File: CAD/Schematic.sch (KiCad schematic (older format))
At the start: 4 parts

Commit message: Resiter value should be equal to the skin resitance value ~2MOhm is great.
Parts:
- removed I?: IDC, symbol Simulation_SPICE:IDC
- added D?: LED, symbol Device:LED
- added LS?: Speaker, symbol Device:Speaker
- added R2: 1M, symbol Device:R
- added U?: 4N35, Package_DIP:DIP-6_W7.62mm, symbol Isolator:4N35
- RotaryEncoder?: symbol OrangeRotaryEncoder:RotaryEncoder -> Schematic-rescue:RotaryEncoder-OrangeRotaryEncoder
- ShockPad?: symbol BhallaLabComponents:ShockPad -> Schematic-rescue:ShockPad-BhallaLabComponents
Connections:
- net labels added: CAM, GND, IMAGING_TRIG, LED, PAD+, PAD-, PUFF, TONE, VCC
- wire segments 8 -> 76
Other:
- note added: "1200 counts per cycle."
- note added: "CH1=CH3 \nCH2=CH4=~CH1\nImplemented in Arduino."
- note added: "PWM"
- note added: "To solenoid."

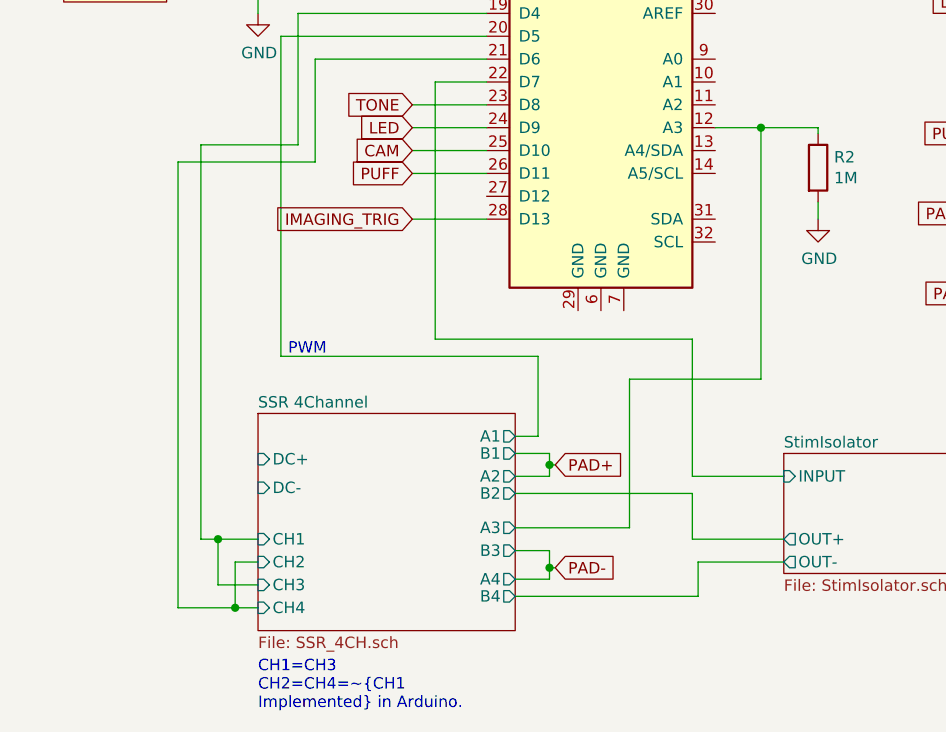
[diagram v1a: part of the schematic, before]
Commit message: Added missing projects.
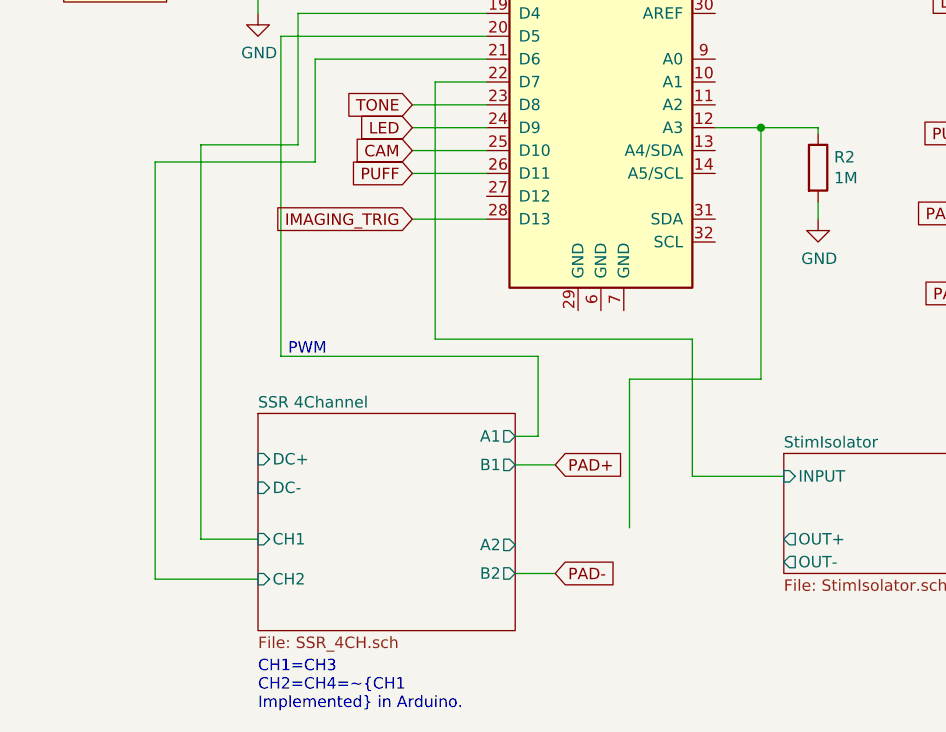
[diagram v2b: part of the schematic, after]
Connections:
- wire segments 76 -> 55
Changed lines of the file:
@@
 Wire Wire Line
 	5800 2900 6300 2900
-$Sheet
-S 5300 4750 1125 950
-U 5D1ADABF
-F0 "SSR 4Channel" 50
-F1 "SSR_4CH.sch" 50
-F2 "DC+" I L 5300 4950 50
-F3 "DC-" I L 5300 5075 50
-F4 "CH1" I L 5300 5300 50
-F5 "CH2" I L 5300 5400 50
-F6 "CH3" I L 5300 5500 50
-F7 "CH4" I L 5300 5600 50
-F8 "A1" O R 6425 4850 50
-F9 "B1" O R 6425 4925 50
-F10 "B2" O R 6425 5100 50
-F11 "A3" O R 6425 5250 50
-F12 "B3" O R 6425 5350 50
-F13 "A4" O R 6425 5475 50
-F14 "B4" O R 6425 5550 50
-F15 "A2" O R 6425 5025 50
-$EndSheet
 $Comp
 L Device:Speaker LS?
@@
 Wire Wire Line
 	5300 2800 5300 3000
-Wire Wire Line
-	5050 5300 5125 5300
-Wire Wire Line
-	5125 5300 5125 5500
-Wire Wire Line
-	5125 5500 5300 5500
-Connection ~ 5125 5300
-Wire Wire Line
-	5125 5300 5300 5300
-Wire Wire Line
-	5300 5400 5200 5400
-Wire Wire Line
-	5200 5400 5200 5600
-Connection ~ 5200 5600
-Wire Wire Line
-	5200 5600 5300 5600
 Text Notes 5300 6050 0    50   ~ 0
 CH1=CH3 \nCH2=CH4=~CH1\nImplemented in Arduino.
@@
 	5550 3200 5550 3650
 Wire Wire Line
-	5550 3650 4950 3650
-Wire Wire Line
-	4950 3650 4950 5600
-Wire Wire Line
 	5550 3200 6300 3200
-Wire Wire Line
-	4950 5600 5200 5600
-Wire Wire Line
-	6425 4925 6575 4925
-Wire Wire Line
-	6575 5025 6425 5025
-Wire Wire Line
-	6425 5350 6575 5350
-Wire Wire Line
-	6575 5475 6425 5475
 Wire Wire Line
 	5400 3100 5400 4500
@@
 Wire Wire Line
 	7500 3500 7300 3500
-Wire Wire Line
-	6575 5350 6575 5425
-Wire Wire Line
-	6575 4925 6575 4975
 $Comp
 L Schematic-rescue:ShockPad-BhallaLabComponents ShockPad?
@@
 Text GLabel 6600 4975 2    50   Input ~ 0
 PAD+
-Text GLabel 6600 5425 2    50   Input ~ 0
-PAD-
-Wire Wire Line
-	6600 4975 6575 4975
-Connection ~ 6575 4975
-Wire Wire Line
-	6575 4975 6575 5025
-Wire Wire Line
-	6600 5425 6575 5425
-Connection ~ 6575 5425
-Wire Wire Line
-	6575 5425 6575 5475
-Wire Wire Line
-	7600 5400 7225 5400
-Wire Wire Line
-	7225 5400 7225 5550
-Wire Wire Line
-	7225 5550 6425 5550
-Wire Wire Line
-	7600 5300 7200 5300
-Wire Wire Line
-	7200 5300 7200 5100
-Wire Wire Line
-	7200 5100 6425 5100
 Wire Wire Line
 	7200 4425 7200 5025
@@
 Wire Wire Line
 	6075 4425 7200 4425
-Wire Wire Line
-	6425 5250 6925 5250
 Wire Wire Line
 	6925 5250 6925 4600
@@
 Text Notes 5600 4500 2    50   ~ 0
 PWM
+Wire Wire Line
+	5050 5300 5300 5300
+Wire Wire Line
+	5300 5475 4850 5475
+Text GLabel 6600 5450 2    50   Input ~ 0
+PAD-
+$Sheet
+S 5300 4750 1125 950
+U 5D1ADABF
+F0 "SSR 4Channel" 50
+F1 "SSR_4CH.sch" 50
+F2 "DC+" I L 5300 4950 50
+F3 "DC-" I L 5300 5075 50
+F4 "CH1" I L 5300 5300 50
+F5 "CH2" I L 5300 5475 50
+F6 "A1" O R 6425 4850 50
+F7 "B1" O R 6425 4975 50
+F8 "B2" O R 6425 5450 50
+F9 "A2" O R 6425 5325 50
+$EndSheet
+Wire Wire Line
+	6425 5450 6600 5450
+Wire Wire Line
+	6425 4975 6600 4975
+Wire Wire Line
+	5550 3650 4850 3650
+Wire Wire Line
+	4850 3650 4850 5475
 $EndSCHEMATC

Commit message: Almost complete.
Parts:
- gave numbers to parts that had none: 2
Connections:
- wire segments 55 -> 73
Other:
- note added: "CH1=CH2 \nCH3=CH4=~CH1\nImplemented in Arduino."
- note added: "Not implemented.\nUsing as black-box."
- note added: "Resistance of mouse's paw is of the order of 1M.\nThe value of R2 must be the same."
- note removed: "CH1=CH3 \nCH2=CH4=~CH1\nImplemented in Arduino."
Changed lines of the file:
@@
 Sheet 1 3
 Title "Shocking Protocol"
-Date ""
-Rev "0.0.1"
-Comp "Bhalla Lab"
-Comment1 ""
-Comment2 ""
-Comment3 ""
+Date "2019-06-30"
+Rev "0.1.0"
+Comp "Bhalla Lab, NCBS Bangalore"
+Comment1 "Shocking protocol for Hrishikesh"
+Comment2 "Stimlus Isolator is not implemented."
+Comment3 "Dilawar Singh, 2019"
 Comment4 ""
 $EndDescr
@@
 	5800 2900 6300 2900
 $Comp
-L Device:Speaker LS?
+L Device:Speaker LS1
 U 1 1 5D18ABCB
 P 8825 2400
-F 0 "LS?" H 8995 2396 50  0000 L CNN
+F 0 "LS1" H 8995 2396 50  0000 L CNN
 F 1 "Speaker" H 8995 2305 50  0000 L CNN
 F 2 "" H 8825 2200 50  0001 C CNN
@@
 $EndComp
 $Comp
-L Device:LED D?
+L Device:LED D1
 U 1 1 5D18B2CE
 P 8775 2950
-F 0 "D?" H 8768 2695 50  0000 C CNN
+F 0 "D1" H 8768 2695 50  0000 C CNN
 F 1 "LED" H 8768 2786 50  0000 C CNN
 F 2 "" H 8775 2950 50  0001 C CNN
@@
 Wire Wire Line
 	8550 2500 8550 2650
-Text Notes 9300 3725 1    50   ~ 10
+Text Notes 9800 3400 2    50   ~ 0
 To solenoid.
 Text Notes 4250 2425 0    50   ~ 0
@@
 	5300 2800 5300 3000
 Text Notes 5300 6050 0    50   ~ 0
-CH1=CH3 \nCH2=CH4=~CH1\nImplemented in Arduino.
+CH1=CH2 \nCH3=CH4=~CH1\nImplemented in Arduino.
 Wire Wire Line
 	5475 3000 5475 3575
 Wire Wire Line
-	5475 3575 5050 3575
-Wire Wire Line
-	5050 3575 5050 5300
+	5475 3575 4900 3575
+Wire Wire Line
+	4900 3575 4900 5300
 Wire Wire Line
 	5475 3000 6300 3000
 Wire Wire Line
-	5550 3200 5550 3650
+	5550 3200 5550 3425
 Wire Wire Line
 	5550 3200 6300 3200
 Wire Wire Line
 	5400 3100 5400 4500
-Wire Wire Line
-	5400 4500 6525 4500
-Wire Wire Line
-	6525 4500 6525 4850
-Wire Wire Line
-	6525 4850 6425 4850
 Wire Wire Line
 	5400 3100 6300 3100
 $Sheet
-S 7600 4925 850  525
+S 7150 5150 850  525
 U 5D191D2C
 F0 "StimIsolator" 50
 F1 "StimIsolator.sch" 50
-F2 "INPUT" I L 7600 5025 50
-F3 "OUT+" O L 7600 5300 50
-F4 "OUT-" O L 7600 5400 50
+F2 "INPUT" I L 7150 5250 50
+F3 "OUT+" O L 7150 5525 50
+F4 "OUT-" O L 7150 5625 50
 $EndSheet
 Wire Wire Line
@@
 Wire Wire Line
 	8475 4225 8975 4225
-Text GLabel 6600 4975 2    50   Input ~ 0
-PAD+
-Wire Wire Line
-	7200 4425 7200 5025
-Wire Wire Line
-	7200 5025 7600 5025
-Wire Wire Line
-	6075 4425 7200 4425
-Wire Wire Line
-	6925 5250 6925 4600
-Wire Wire Line
-	6925 4600 7500 4600
+Wire Wire Line
+	6075 4425 7000 4425
 Wire Wire Line
 	7500 4600 7500 3500
@@
 PWM
 Wire Wire Line
-	5050 5300 5300 5300
-Wire Wire Line
-	5300 5475 4850 5475
-Text GLabel 6600 5450 2    50   Input ~ 0
-PAD-
+	4900 5300 5300 5300
 $Sheet
 S 5300 4750 1125 950
@@
 F3 "DC-" I L 5300 5075 50
 F4 "CH1" I L 5300 5300 50
-F5 "CH2" I L 5300 5475 50
+F5 "CH2" I L 5300 5400 50
 F6 "A1" O R 6425 4850 50
-F7 "B1" O R 6425 4975 50
-F8 "B2" O R 6425 5450 50
-F9 "A2" O R 6425 5325 50
+F7 "B1" O R 6425 4925 50
+F8 "B2" O R 6425 5100 50
+F9 "A2" O R 6425 5025 50
+F10 "CH3" I L 5300 5525 50
+F11 "CH4" I L 5300 5625 50
+F12 "A3" O R 6425 5325 50
+F13 "B3" O R 6425 5400 50
+F14 "A4" O R 6425 5525 50
+F15 "B4" O R 6425 5600 50
 $EndSheet
 Wire Wire Line
-	6425 5450 6600 5450
-Wire Wire Line
-	6425 4975 6600 4975
-Wire Wire Line
-	5550 3650 4850 3650
-Wire Wire Line
-	4850 3650 4850 5475
+	5400 4500 6525 4500
+Wire Wire Line
+	6525 4500 6525 4850
+Wire Wire Line
+	6525 4850 6425 4850
+Wire Wire Line
+	6925 4600 7500 4600
+Wire Wire Line
+	6925 5025 6925 4600
+Wire Wire Line
+	5550 3425 4825 3425
+Text GLabel 6550 4925 2    50   Input ~ 0
+PAD+
+Wire Wire Line
+	6425 4925 6550 4925
+Wire Wire Line
+	4900 5300 4900 5400
+Wire Wire Line
+	4900 5400 5300 5400
+Connection ~ 4900 5300
+Wire Wire Line
+	4825 5525 4900 5525
+Wire Wire Line
+	4825 3425 4825 5525
+Wire Wire Line
+	4900 5525 4900 5625
+Wire Wire Line
+	4900 5625 5300 5625
+Connection ~ 4900 5525
+Wire Wire Line
+	4900 5525 5300 5525
+Wire Wire Line
+	6925 5025 6425 5025
+Text GLabel 6550 5100 2    50   Input ~ 0
+PAD-
+Wire Wire Line
+	6425 5100 6550 5100
+Text GLabel 6550 5400 2    50   Input ~ 0
+PAD+
+Text GLabel 6550 5600 2    50   Input ~ 0
+PAD-
+Wire Wire Line
+	6425 5400 6550 5400
+Wire Wire Line
+	6425 5600 6550 5600
+Wire Wire Line
+	7000 4425 7000 5250
+Wire Wire Line
+	7150 5250 7000 5250
+Wire Wire Line
+	7150 5525 6875 5525
+Wire Wire Line
+	6875 5525 6875 5325
+Wire Wire Line
+	6875 5325 6425 5325
+Wire Wire Line
+	7150 5625 6825 5625
+Wire Wire Line
+	6825 5625 6825 5525
+Wire Wire Line
+	6825 5525 6425 5525
+Text Notes 8175 5450 2    50   ~ 0
+Not implemented.\nUsing as black-box.
+Text Notes 10200 4525 2    50   ~ 0
+Resistance of mouse's paw is of the order of 1M.\nThe value of R2 must be the same.
+$Comp
+L power:VCC #PWR?
+U 1 1 5D206B22
+P 5100 4900
+F 0 "#PWR?" H 5100 4750 50  0001 C CNN
+F 1 "VCC" H 5117 5073 50  0000 C CNN
+F 2 "" H 5100 4900 50  0001 C CNN
+F 3 "" H 5100 4900 50  0001 C CNN
+	1    5100 4900
+	1    0    0    -1
+$EndComp
+$Comp
+L power:GND #PWR?
+U 1 1 5D208D90
+P 5125 5100
+F 0 "#PWR?" H 5125 4850 50  0001 C CNN
+F 1 "GND" H 5130 4927 50  0000 C CNN
+F 2 "" H 5125 5100 50  0001 C CNN
+F 3 "" H 5125 5100 50  0001 C CNN
+	1    5125 5100
+	1    0    0    -1
+$EndComp
+Wire Wire Line
+	5300 5075 5125 5075
+Wire Wire Line
+	5125 5075 5125 5100
+Wire Wire Line
+	5300 4950 5100 4950
+Wire Wire Line
+	5100 4950 5100 4900
 $EndSCHEMATC

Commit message: Some renames.
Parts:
- gave numbers to parts that had none: 3
- renumbered ArduinoUno to ArduinoUno1
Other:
- moved on the sheet: ArduinoUno1, D1, LS1, R2, U1

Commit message: Added RC tank to get the RMS value. R=1.2 MOhm C=47 nF. Tau ~50mS
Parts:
- added CA3: 47nF, symbol Device:C
- RA3: renamed from R2; value 1M -> 1.2 M
- RotaryEncoder1: symbol Schematic-rescue:RotaryEncoder-OrangeRotaryEncoder -> Schematic-rescue:RotaryEncoder-OrangeRotaryEncoder-Schematic-rescue
- ShockPad1: symbol Schematic-rescue:ShockPad-BhallaLabComponents -> Schematic-rescue:ShockPad-BhallaLabComponents-Schematic-rescue
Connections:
- wire segments 73 -> 77
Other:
- note added: "D5, PWM, 20 kHz"
- note removed: "PWM"
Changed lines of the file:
@@
 $EndComp
 $Comp
-L Schematic-rescue:RotaryEncoder-OrangeRotaryEncoder RotaryEncoder1
+L Schematic-rescue:RotaryEncoder-OrangeRotaryEncoder-Schematic-rescue RotaryEncoder1
 U 1 1 5D191567
 P 2750 2450
@@
 	5600 3250 5400 3250
 $Comp
-L Schematic-rescue:ShockPad-BhallaLabComponents ShockPad1
+L Schematic-rescue:ShockPad-BhallaLabComponents-Schematic-rescue ShockPad1
 U 1 1 5D197A8E
 P 7525 3775
@@
 	5600 4350 5600 3250
 $Comp
-L Device:R R2
+L Device:R RA3
 U 1 1 5D1B22CC
 P 5850 3425
-F 0 "R2" H 5920 3471 50  0000 L CNN
-F 1 "1M" H 5920 3380 50  0000 L CNN
+F 0 "RA3" V 5920 3471 50  0000 L CNN
+F 1 "1.2 M" H 5920 3380 50  0000 R TNN
 F 2 "" V 5780 3425 50  0001 C CNN
 F 3 "~" H 5850 3425 50  0001 C CNN
 	1    5850 3425
-	1    0    0    -1
+	-1   0    0    1
 $EndComp
 $Comp
@@
 $EndComp
 Wire Wire Line
-	5850 3575 5850 3650
+	5850 3575 5850 3600
 Wire Wire Line
 	5850 3275 5850 3250
@@
 	5850 3250 5600 3250
 Connection ~ 5600 3250
-Text Notes 3700 4250 2    50   ~ 0
-PWM
+Text Notes 3700 4250 0    50   ~ 0
+D5, PWM, 20 kHz
 Wire Wire Line
 	3000 5050 3400 5050
@@
 Wire Wire Line
 	3200 4700 3200 4650
+$Comp
+L Device:C CA3
+U 1 1 5D1B6EF2
+P 6100 3450
+F 0 "CA3" H 6215 3496 50  0000 L CNN
+F 1 "47nF" H 6215 3405 50  0000 L CNN
+F 2 "" H 6138 3300 50  0001 C CNN
+F 3 "~" H 6100 3450 50  0001 C CNN
+	1    6100 3450
+	1    0    0    -1
+$EndComp
+Wire Wire Line
+	6100 3300 6100 3250
+Wire Wire Line
+	6100 3250 5850 3250
+Connection ~ 5850 3250
+Wire Wire Line
+	6100 3600 5850 3600
+Connection ~ 5850 3600
+Wire Wire Line
+	5850 3600 5850 3650
 $EndSCHEMATC

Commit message: upgraded design.
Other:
- note added: "Low Level Trigger.\nVendor: NA \nAsk hrishi@ncbs.res.in"
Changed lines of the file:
@@
 Wire Wire Line
 	3000 5050 3400 5050
-$Sheet
-S 3400 4500 1125 950
-U 5D1ADABF
-F0 "SSR 4Channel" 50
-F1 "SSR_4CH.sch" 50
-F2 "DC+" I L 3400 4700 50
-F3 "DC-" I L 3400 4825 50
-F4 "CH1" I L 3400 5050 50
-F5 "CH2" I L 3400 5150 50
-F6 "A1" O R 4525 4600 50
-F7 "B1" O R 4525 4675 50
-F8 "B2" O R 4525 4850 50
-F9 "A2" O R 4525 4775 50
-F10 "CH3" I L 3400 5275 50
-F11 "CH4" I L 3400 5375 50
-F12 "A3" O R 4525 5075 50
-F13 "B3" O R 4525 5150 50
-F14 "A4" O R 4525 5275 50
-F15 "B4" O R 4525 5350 50
-$EndSheet
 Wire Wire Line
 	3500 4250 4625 4250
@@
 Wire Wire Line
 	5850 3600 5850 3650
+$Sheet
+S 3400 4500 1125 950
+U 5D1ADABF
+F0 "SSR 4Ch" 50
+F1 "SSR_4CH.sch" 50
+F2 "DC+" I L 3400 4700 50
+F3 "DC-" I L 3400 4825 50
+F4 "CH1" I L 3400 5050 50
+F5 "CH2" I L 3400 5150 50
+F6 "A1" O R 4525 4600 50
+F7 "B1" O R 4525 4675 50
+F8 "B2" O R 4525 4850 50
+F9 "A2" O R 4525 4775 50
+F10 "CH3" I L 3400 5275 50
+F11 "CH4" I L 3400 5375 50
+F12 "A3" O R 4525 5075 50
+F13 "B3" O R 4525 5150 50
+F14 "A4" O R 4525 5275 50
+F15 "B4" O R 4525 5350 50
+$EndSheet
+Text Notes 3600 5000 0    50   ~ 0
+Low Level Trigger.\nVendor: NA \nAsk hrishi@ncbs.res.in
 $EndSCHEMATC
